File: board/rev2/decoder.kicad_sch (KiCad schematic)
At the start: 4 parts, among them U10 74VHC161

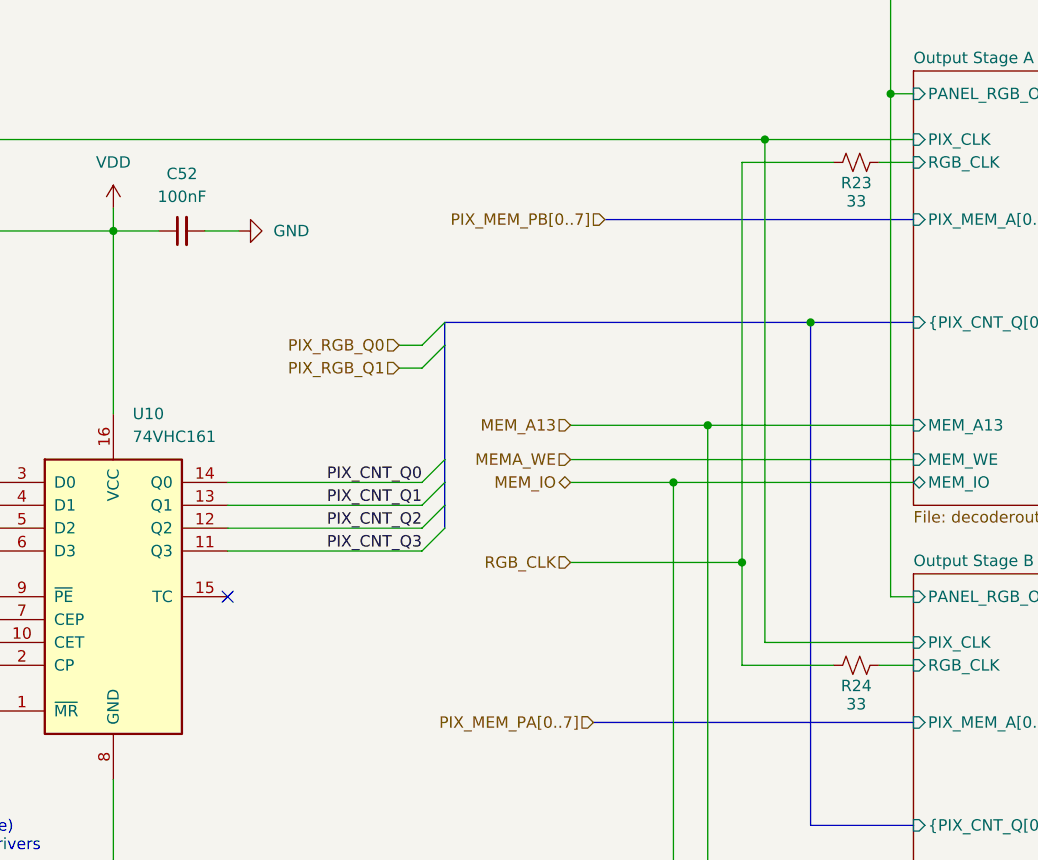
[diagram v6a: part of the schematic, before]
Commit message: Really finish rev2 board schematic
- fix some more footprints
  - move to real SD card holder, for example
- repair part numbers
- add LCSC part refs to everything
- add even more caps to the 3.3V reg output
  - really should use an LDO but meh it should be fine

total BOM cost for 5 of them is apparently 160 CAD, or like 32 dollars
each (don't think that includes the feeder fees tho)
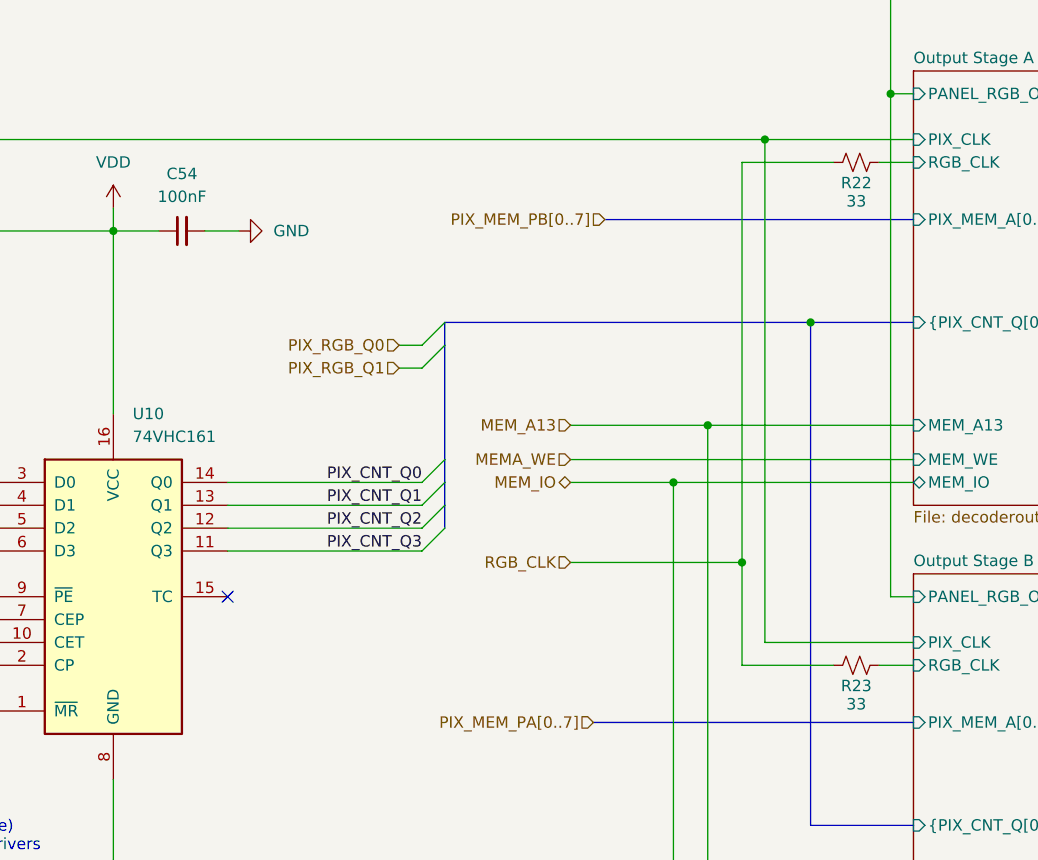
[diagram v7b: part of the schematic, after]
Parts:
- C54: renamed from C52; LCSC (none) -> C307331
- R22: renamed from R23; LCSC (none) -> C25105
- R23: renamed from R24; LCSC (none) -> C25105
- U10: LCSC (none) -> C7421276; Part 74VHC161 -> 74VHC161FT(BJ)
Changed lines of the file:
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@@
 			)
 		)
-		(property "Part" "74VHC161"
+		(property "Part" "74VHC161FT(BJ)"
+			(at 91.44 99.06 0)
+			(effects
+				(font
+					(size 1.27 1.27)
+				)
+				(hide yes)
+			)
+		)
+		(property "LCSC" "C7421276"
 			(at 91.44 99.06 0)
 			(effects
@@
 		(on_board yes)
 		(dnp no)
-		(property "Reference" "R23"
+		(property "Reference" "R22"
 			(at 173.99 53.086 90)
 			(effects
@@
 			)
 		)
+		(property "LCSC" "C25105"
+			(at 173.99 50.8 90)
+			(effects
+				(font
+					(size 1.27 1.27)
+				)
+				(hide yes)
+			)
+		)
 		(pin "2"
 		)
@@
 			(project "mainboard"
 				(path "/32eb05c7-b4a6-42f3-8fb3-43453631100f/2c9586de-ca2f-4a0b-8ff8-8fdad1d1abcc"
-					(reference "R23")
+					(reference "R22")
 					(unit 1)
 				)
@@
 		(dnp no)
 		(fields_autoplaced yes)
-		(property "Reference" "C52"
+		(property "Reference" "C54"
 			(at 99.0663 52.07 90)
 			(effects
@@
 			)
 		)
+		(property "LCSC" "C307331 "
+			(at 99.06 58.42 90)
+			(effects
+				(font
+					(size 1.27 1.27)
+				)
+				(hide yes)
+			)
+		)
 		(pin "2"
 		)
@@
 			(project ""
 				(path "/32eb05c7-b4a6-42f3-8fb3-43453631100f/2c9586de-ca2f-4a0b-8ff8-8fdad1d1abcc"
-					(reference "C52")
+					(reference "C54")
 					(unit 1)
 				)
@@
 		(dnp no)
 		(fields_autoplaced yes)
-		(property "Reference" "#PWR034"
+		(property "Reference" "#PWR035"
 			(at 111.76 58.42 0)
 			(effects
@@
 			(project ""
 				(path "/32eb05c7-b4a6-42f3-8fb3-43453631100f/2c9586de-ca2f-4a0b-8ff8-8fdad1d1abcc"
-					(reference "#PWR034")
+					(reference "#PWR035")
 					(unit 1)
 				)
@@
 		(on_board yes)
 		(dnp no)
-		(property "Reference" "R24"
+		(property "Reference" "R23"
 			(at 173.99 108.966 90)
 			(effects
@@
 			)
 		)
+		(property "LCSC" "C25105"
+			(at 173.99 106.68 90)
+			(effects
+				(font
+					(size 1.27 1.27)
+				)
+				(hide yes)
+			)
+		)
 		(pin "2"
 		)
@@
 			(project ""
 				(path "/32eb05c7-b4a6-42f3-8fb3-43453631100f/2c9586de-ca2f-4a0b-8ff8-8fdad1d1abcc"
-					(reference "R24")
+					(reference "R23")
 					(unit 1)
 				)
@@
 		(dnp no)
 		(fields_autoplaced yes)
-		(property "Reference" "#PWR033"
+		(property "Reference" "#PWR034"
 			(at 91.44 134.62 0)
 			(effects
@@
 			(project "mainboard"
 				(path "/32eb05c7-b4a6-42f3-8fb3-43453631100f/2c9586de-ca2f-4a0b-8ff8-8fdad1d1abcc"
-					(reference "#PWR033")
+					(reference "#PWR034")
 					(unit 1)
 				)
@@
 		(dnp no)
 		(fields_autoplaced yes)
-		(property "Reference" "#PWR032"
+		(property "Reference" "#PWR033"
 			(at 91.44 59.69 0)
 			(effects
@@
 			(project "mainboard"
 				(path "/32eb05c7-b4a6-42f3-8fb3-43453631100f/2c9586de-ca2f-4a0b-8ff8-8fdad1d1abcc"
-					(reference "#PWR032")
-					(unit 1)
-				)
+					(reference "#PWR033")
+					(unit 1)
+				)

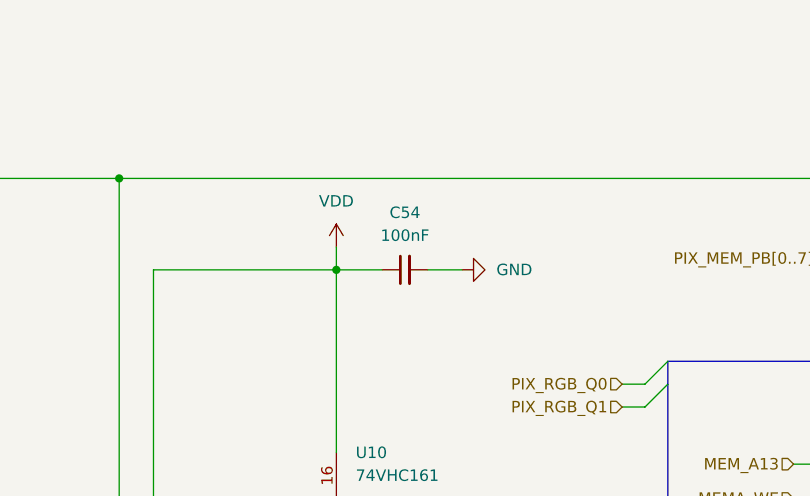
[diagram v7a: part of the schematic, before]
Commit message: Start board
add a few extra bypass caps too, and swap some pins on the USB mux

i forgot to add a bypass cap on the tpd6s so that also needs to happen

truly 63 capacitors is not enough
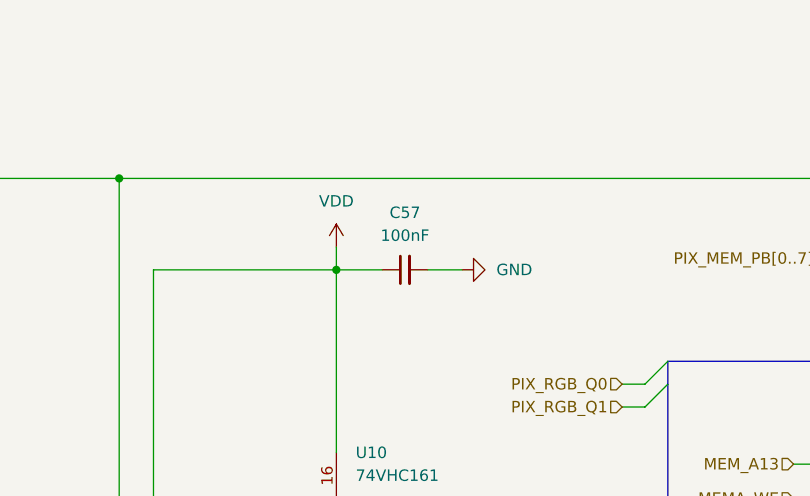
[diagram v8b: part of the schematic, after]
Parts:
- renumbered C54 to C57
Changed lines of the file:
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@@
 		(dnp no)
 		(fields_autoplaced yes)
-		(property "Reference" "C54"
+		(property "Reference" "C57"
 			(at 99.0663 52.07 90)
 			(effects
@@
 			(project ""
 				(path "/32eb05c7-b4a6-42f3-8fb3-43453631100f/2c9586de-ca2f-4a0b-8ff8-8fdad1d1abcc"
-					(reference "C54")
+					(reference "C57")
 					(unit 1)
 				)
@@
 		(dnp no)
 		(fields_autoplaced yes)
-		(property "Reference" "#PWR035"
+		(property "Reference" "#PWR036"
 			(at 111.76 58.42 0)
 			(effects
@@
 			(project ""
 				(path "/32eb05c7-b4a6-42f3-8fb3-43453631100f/2c9586de-ca2f-4a0b-8ff8-8fdad1d1abcc"
-					(reference "#PWR035")
+					(reference "#PWR036")
 					(unit 1)
 				)
@@
 		(dnp no)
 		(fields_autoplaced yes)
-		(property "Reference" "#PWR034"
+		(property "Reference" "#PWR035"
 			(at 91.44 134.62 0)
 			(effects
@@
 			(project "mainboard"
 				(path "/32eb05c7-b4a6-42f3-8fb3-43453631100f/2c9586de-ca2f-4a0b-8ff8-8fdad1d1abcc"
-					(reference "#PWR034")
+					(reference "#PWR035")
 					(unit 1)
 				)
@@
 		(dnp no)
 		(fields_autoplaced yes)
-		(property "Reference" "#PWR033"
+		(property "Reference" "#PWR034"
 			(at 91.44 59.69 0)
 			(effects
@@
 			(project "mainboard"
 				(path "/32eb05c7-b4a6-42f3-8fb3-43453631100f/2c9586de-ca2f-4a0b-8ff8-8fdad1d1abcc"
-					(reference "#PWR033")
-					(unit 1)
-				)
+					(reference "#PWR034")
+					(unit 1)
+				)
